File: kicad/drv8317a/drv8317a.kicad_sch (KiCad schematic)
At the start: 0 parts

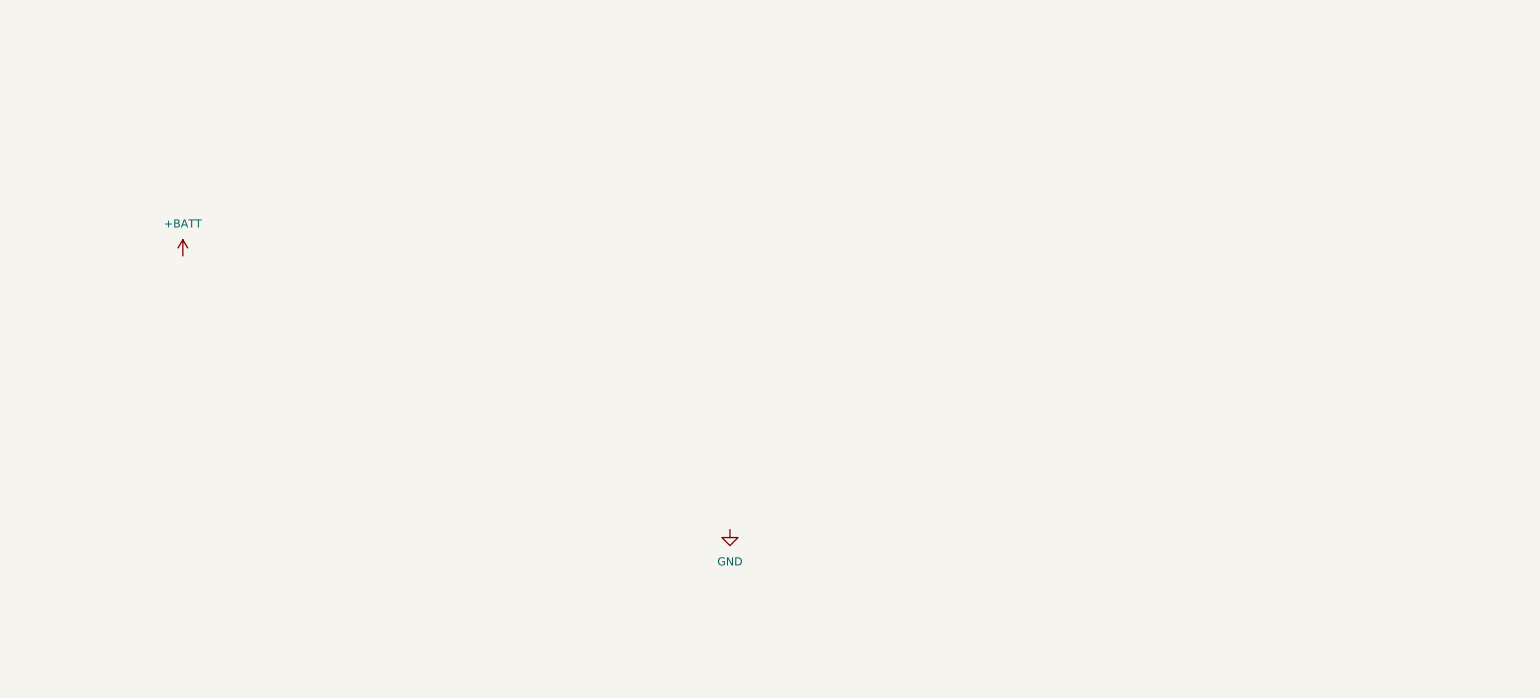
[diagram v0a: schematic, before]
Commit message: added DRV8317
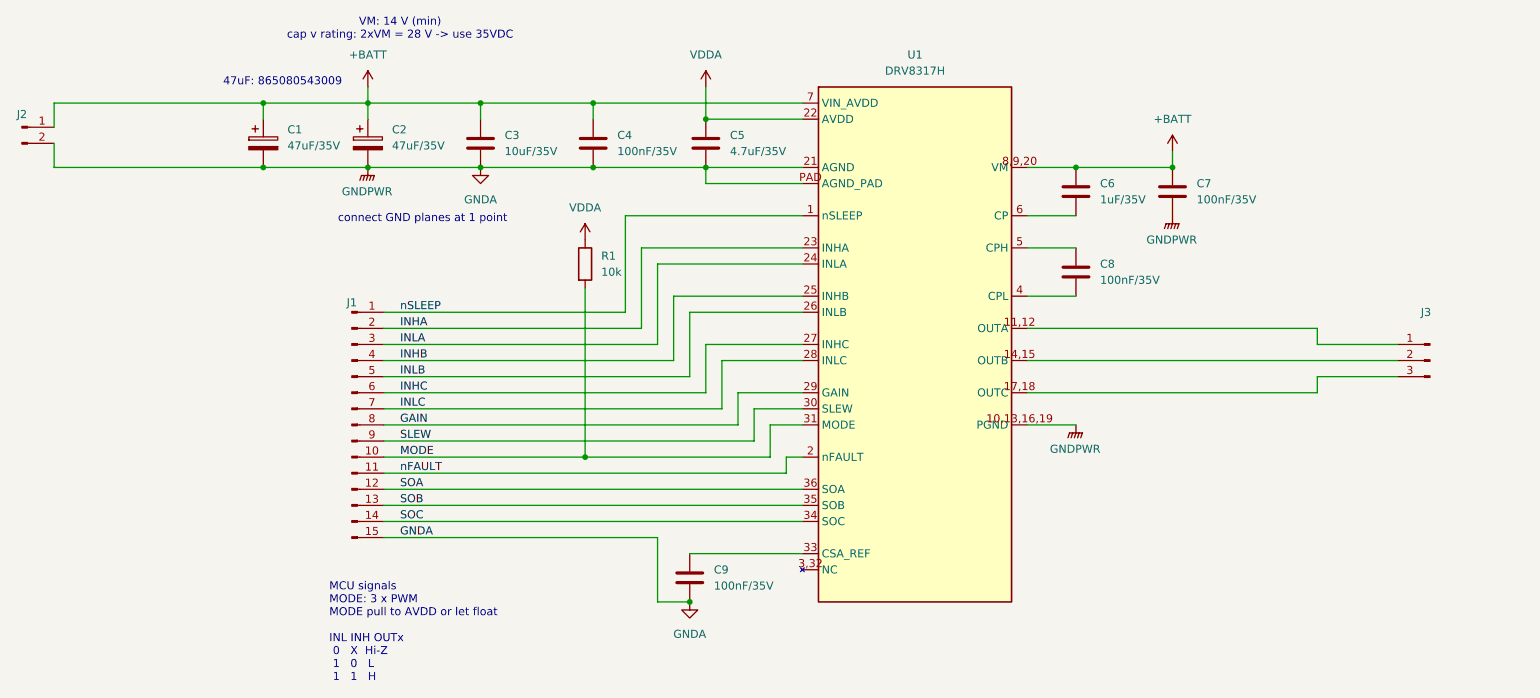
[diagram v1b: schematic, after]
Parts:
- added C1, C2: 47uF/35V, symbol Device:C_Polarized
- added C3: 10uF/35V, symbol Device:C
- added C4, C7, C8, C9: 100nF/35V, symbol Device:C
- added C5: 4.7uF/35V, symbol Device:C
- added C6: 1uF/35V, symbol Device:C
- added J1: Conn_01x15_Pin, symbol Connector:Conn_01x15_Pin
- added J2: Conn_01x02_Pin, symbol Connector:Conn_01x02_Pin
- added J3: Conn_01x03_Pin, symbol Connector:Conn_01x03_Pin
- added R1: 10k, symbol Device:R
- added U1: DRV8317H, symbol bldc-driver-lib:DRV8317H
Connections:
- net +BATT: now also C1.1, C2.1, C3.1, C4.1, C6.1, C7.1, J2.1 (Pin_1), U1.7 (VIN_AVDD), U1.8,9,20 (VM)
- new net: C6.2, U1.6 (CP)
- new net: J3.1 (Pin_1), U1.11,12 (OUTA)
- new net: J3.2 (Pin_2), U1.14,15 (OUTB)
- new net: J3.3 (Pin_3), U1.17,18 (OUTC)
- new net: C9.1, U1.33 (CSA_REF)
- new net: C8.2, U1.4 (CPL)
- new net: C8.1, U1.5 (CPH)
- new net GAIN: J1.8 (Pin_8), U1.29 (GAIN)
- new net GNDA: C1.2, C2.2, C3.2, C4.2, C5.2, C7.2, C9.2, J1.15 (Pin_15), J2.2 (Pin_2), U1.10,13,16,19 (PGND), U1.21 (AGND), U1.PAD (AGND_PAD)
- new net INHA: J1.2 (Pin_2), U1.23 (INHA)
- new net INHB: J1.4 (Pin_4), U1.25 (INHB)
- new net INHC: J1.6 (Pin_6), U1.27 (INHC)
- new net INLA: J1.3 (Pin_3), U1.24 (INLA)
- new net INLB: J1.5 (Pin_5), U1.26 (INLB)
- new net INLC: J1.7 (Pin_7), U1.28 (INLC)
- new net MODE: J1.10 (Pin_10), R1.2, U1.31 (MODE)
- new net SLEW: J1.9 (Pin_9), U1.30 (SLEW)
- new net SOA: J1.12 (Pin_12), U1.36 (SOA)
- new net SOB: J1.13 (Pin_13), U1.35 (SOB)
- new net SOC: J1.14 (Pin_14), U1.34 (SOC)
- new net VDDA: C5.1, R1.1, U1.22 (AVDD)
- new net nFAULT: J1.11 (Pin_11), U1.2 (nFAULT)
- new net nSLEEP: J1.1 (Pin_1), U1.1 (nSLEEP)
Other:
- note added: "47uF: 865080543009"
- note added: "MCU signals MODE: 3 x PWM MODE pull to AVDD or let float INL INH OUTx 0 X Hi-Z 1 0 L 1 1 H"
- note added: "VM: 14 V (min) cap v rating: 2xVM = 28 V -> use 35VDC"
- note added: "connect GND planes at 1 point"

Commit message: WQFN 36 Footprint added
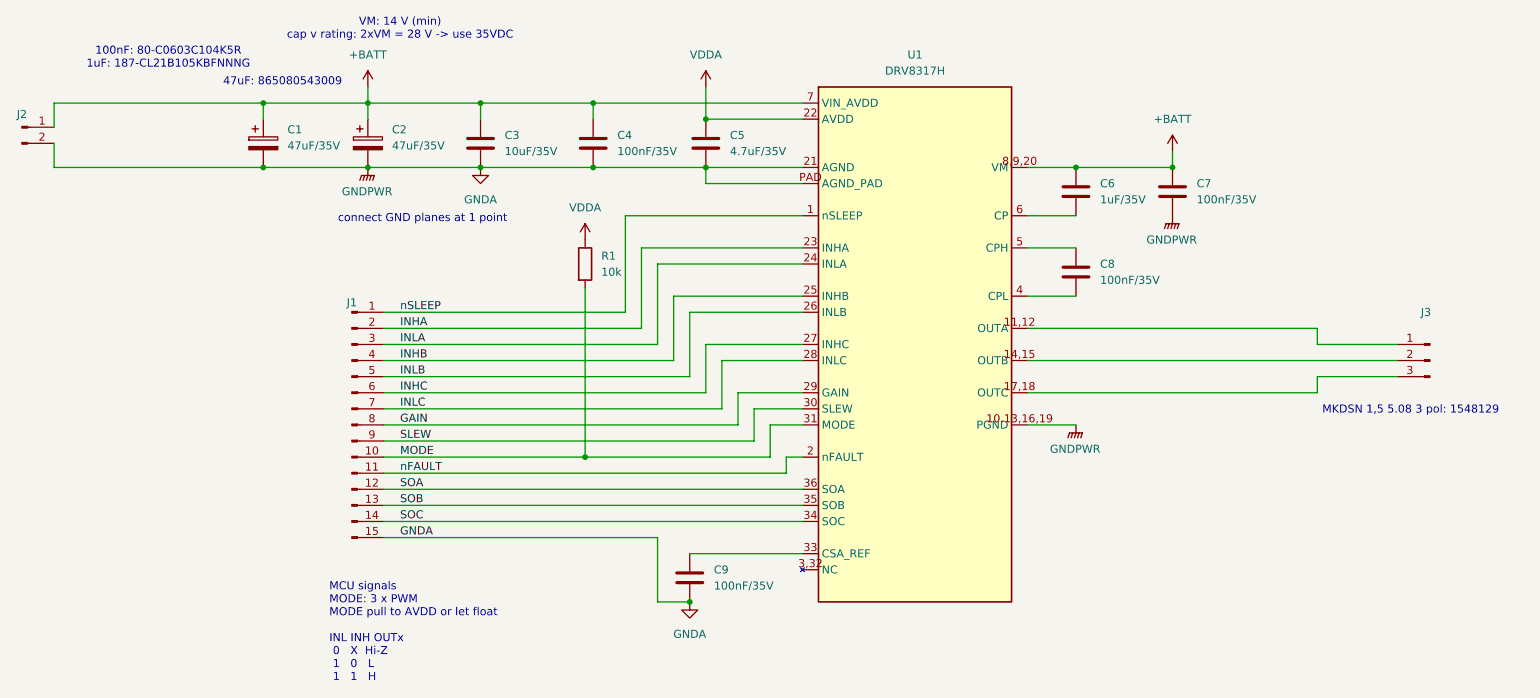
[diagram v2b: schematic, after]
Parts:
- C1, C2: footprint (none) -> Capacitor_SMD:CP_Elec_6.3x7.7
- C3, C5, C6: footprint (none) -> Capacitor_SMD:C_0805_2012Metric_Pad1.18x1.45mm_HandSolder
- C4, C7, C8, C9: footprint (none) -> Capacitor_SMD:C_0603_1608Metric_Pad1.08x0.95mm_HandSolder
- J1: footprint (none) -> Connector_PinHeader_2.54mm:PinHeader_1x15_P2.54mm_Vertical
- J2: footprint (none) -> Connector_PinHeader_2.54mm:PinHeader_1x02_P2.54mm_Vertical
- J3: footprint (none) -> TerminalBlock_Phoenix:TerminalBlock_Phoenix_MKDS-1,5-3-5.08_1x03_P5.08mm_Horizontal
- R1: footprint (none) -> Resistor_SMD:R_0603_1608Metric_Pad0.98x0.95mm_HandSolder
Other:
- note added: "100nF: 80-C0603C104K5R 1uF: 187-CL21B105KBFNNNG"
- note added: "MKDSN 1,5 5.08 3 pol: 1548129"
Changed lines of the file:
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@@
+		)
+	)
+	(text "MKDSN 1,5 5.08 3 pol: 1548129"
+		(exclude_from_sim no)
+		(at 245.872 94.234 0)
+		(effects
+			(font
+				(size 1.27 1.27)
+			)
 		)
 	)
@@
 		(exclude_from_sim no)
 		(at 67.818 42.418 0)
+		(effects
+			(font
+				(size 1.27 1.27)
+			)
+		)
+	)
+	(text "100nF: 80-C0603C104K5R\n1uF: 187-CL21B105KBFNNNG\n"
+		(exclude_from_sim no)
+		(at 49.784 38.608 0)
 		(effects
 			(font
@@
 			)
 		)
-		(property "Footprint" ""
+		(property "Footprint" "Capacitor_SMD:CP_Elec_6.3x7.7"
 			(at 65.7352 55.88 0)
 			(effects
@@
 			)
 		)
-		(property "Footprint" ""
+		(property "Footprint" "Capacitor_SMD:C_0805_2012Metric_Pad1.18x1.45mm_HandSolder"
 			(at 194.0052 63.5 0)
 			(effects
@@
 			)
 		)
-		(property "Footprint" ""
+		(property "Footprint" "Capacitor_SMD:C_0603_1608Metric_Pad1.08x0.95mm_HandSolder"
 			(at 117.8052 55.88 0)
 			(effects
@@
 			)
 		)
-		(property "Footprint" ""
+		(property "Footprint" "TerminalBlock_Phoenix:TerminalBlock_Phoenix_MKDS-1,5-3-5.08_1x03_P5.08mm_Horizontal"
 			(at 248.92 86.36 0)
 			(effects
@@
 			)
 		)
-		(property "Footprint" ""
+		(property "Footprint" "Capacitor_SMD:C_0805_2012Metric_Pad1.18x1.45mm_HandSolder"
 			(at 135.5852 55.88 0)
 			(effects
@@
 			)
 		)
-		(property "Footprint" ""
+		(property "Footprint" "Capacitor_SMD:C_0603_1608Metric_Pad1.08x0.95mm_HandSolder"
 			(at 209.2452 63.5 0)
 			(effects
@@
 			)
 		)
-		(property "Footprint" ""
+		(property "Footprint" "Connector_PinHeader_2.54mm:PinHeader_1x15_P2.54mm_Vertical"
 			(at 78.74 96.52 0)
 			(effects
@@
 			)
 		)
-		(property "Footprint" ""
+		(property "Footprint" "Capacitor_SMD:C_0603_1608Metric_Pad1.08x0.95mm_HandSolder"
 			(at 133.0452 124.46 0)
 			(effects
@@
 			)
 		)
-		(property "Footprint" ""
+		(property "Footprint" "Capacitor_SMD:CP_Elec_6.3x7.7"
 			(at 82.2452 55.88 0)
 			(effects
@@
 			)
 		)
-		(property "Footprint" ""
+		(property "Footprint" "Capacitor_SMD:C_0805_2012Metric_Pad1.18x1.45mm_HandSolder"
 			(at 100.0252 55.88 0)
 			(effects
@@
 			)
 		)
-		(property "Footprint" ""
+		(property "Footprint" "Resistor_SMD:R_0603_1608Metric_Pad0.98x0.95mm_HandSolder"
 			(at 113.792 71.12 90)
 			(effects
@@
 			)
 		)
-		(property "Footprint" ""
+		(property "Footprint" "Connector_PinHeader_2.54mm:PinHeader_1x02_P2.54mm_Vertical"
 			(at 26.67 49.53 0)
 			(effects
@@
 			)
 		)
-		(property "Footprint" ""
+		(property "Footprint" "Capacitor_SMD:C_0603_1608Metric_Pad1.08x0.95mm_HandSolder"
 			(at 194.0052 76.2 0)
 			(effects

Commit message: pcb started
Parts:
- removed C2: 47uF/35V, Capacitor_SMD:CP_Elec_6.3x7.7, symbol Device:C_Polarized
- removed J1: Conn_01x15_Pin, Connector_PinHeader_2.54mm:PinHeader_1x15_P2.54mm_Vertical, symbol Connector:Conn_01x15_Pin
- added J1: Conn_01x08_Pin, Connector_PinHeader_2.54mm:PinHeader_1x08_P2.54mm_Vertical, symbol Connector:Conn_01x08_Pin
- added J4: Conn_01x06_Pin, Connector_PinHeader_2.54mm:PinHeader_1x06_P2.54mm_Vertical, symbol Connector:Conn_01x06_Pin
- added NT1: NetTie_2, NetTie:NetTie-2_SMD_Pad2.0mm, symbol Device:NetTie_2
- U1: footprint (none) -> bldc-driver-lib:WQFN-36_EP_4.4x5.4_Pitch0.4mm
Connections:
- net INLB is gone; now on net INL: U1.26 (INLB)
- net INLC is gone; now on net INL: U1.28 (INLC)
- net +BATT: now also U1.20 (VM), U1.8 (VM), U1.9 (VM); no longer U1.8,9,20 (VM)
- net GAIN: now also J1.6 (Pin_6)
- net GNDA: now also U1.37 (AGND_PAD), J4.5 (Pin_5), J4.6 (Pin_6), NT1.2; no longer C1.2, C7.2, J2.2 (Pin_2), U1.10,13,16,19 (PGND), U1.PAD (AGND_PAD)
- net INHA: now also J1.2 (Pin_2)
- net INHB: now also J1.3 (Pin_3)
- net INHC: now also J1.4 (Pin_4)
- net MODE: now also J1.8 (Pin_8)
- net SLEW: now also J1.7 (Pin_7)
- net SOA: now also J4.2 (Pin_2)
- net SOB: now also J4.3 (Pin_3)
- net SOC: now also J4.4 (Pin_4)
- net nFAULT: now also J4.1 (Pin_1)
- net nSLEEP: now also J1.1 (Pin_1)
- net OUTA: now reaches J3.1 (Pin_1)
- net OUTA: now also U1.11 (OUTA), U1.12 (OUTA); no longer U1.11,12 (OUTA)
- net OUTB: now reaches J3.2 (Pin_2)
- net OUTB: now also U1.14 (OUTB), U1.15 (OUTB); no longer U1.14,15 (OUTB)
- net OUTC: now reaches J3.3 (Pin_3)
- net OUTC: now also U1.17 (OUTC), U1.18 (OUTC); no longer U1.17,18 (OUTC)
- net INLA renamed INL
- net INL: now also J1.5 (Pin_5)
- new net GNDPWR: C1.2, C7.2, J2.2 (Pin_2), NT1.1, U1.10 (PGND), U1.13 (PGND), U1.16 (PGND), U1.19 (PGND)
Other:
- moved on the sheet: C1, J2, J3, R1

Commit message: 100% routed, review needed
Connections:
- net GAIN: now also J1.5 (Pin_5); no longer J1.6 (Pin_6)
- net INHA: now also J1.1 (Pin_1); no longer J1.2 (Pin_2)
- net INHB: now also J1.2 (Pin_2); no longer J1.3 (Pin_3)
- net INHC: now also J1.3 (Pin_3); no longer J1.4 (Pin_4)
- net INL: now also J1.4 (Pin_4); no longer J1.5 (Pin_5)
- net MODE: now also J1.7 (Pin_7); no longer J1.8 (Pin_8)
- net SLEW: now also J1.6 (Pin_6); no longer J1.7 (Pin_7)
- net nSLEEP: now also J1.8 (Pin_8); no longer J1.1 (Pin_1)

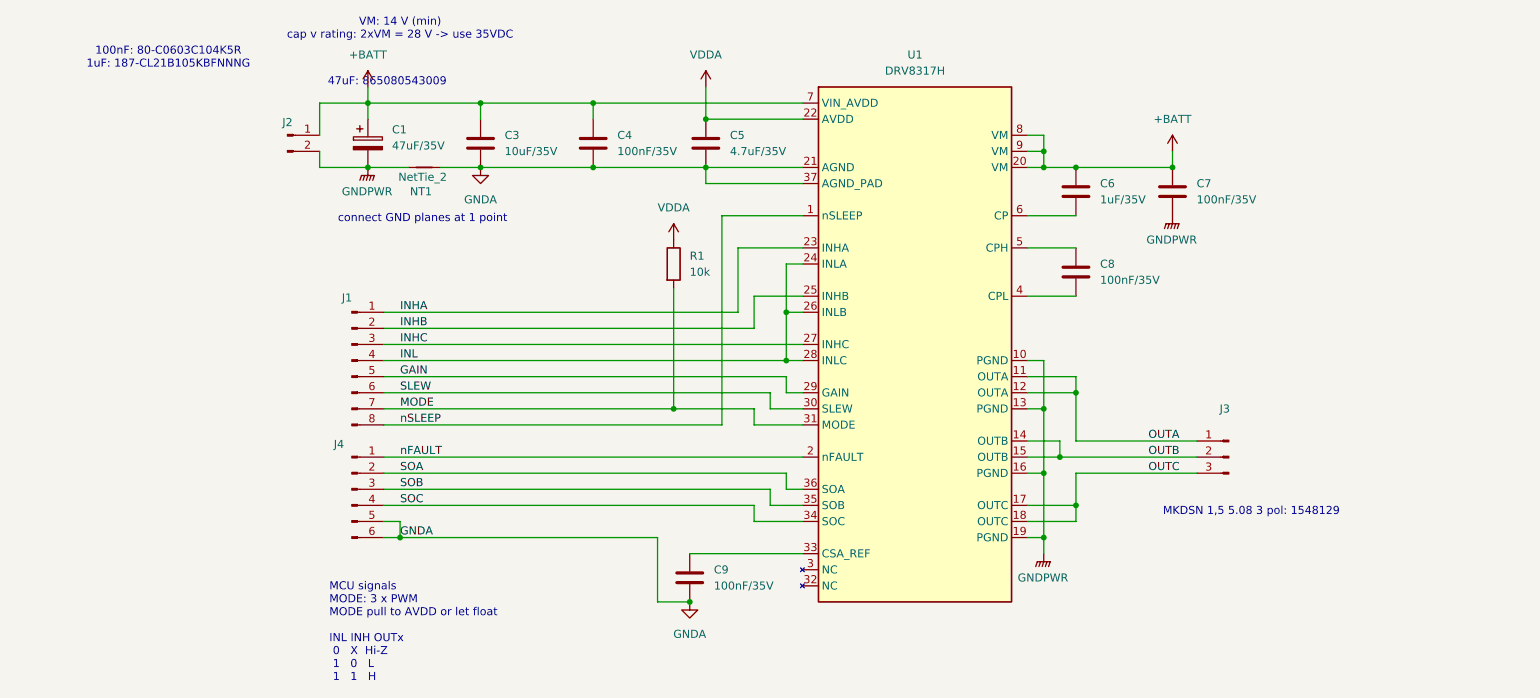
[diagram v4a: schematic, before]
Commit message: config: use resistors instead of mcu signals
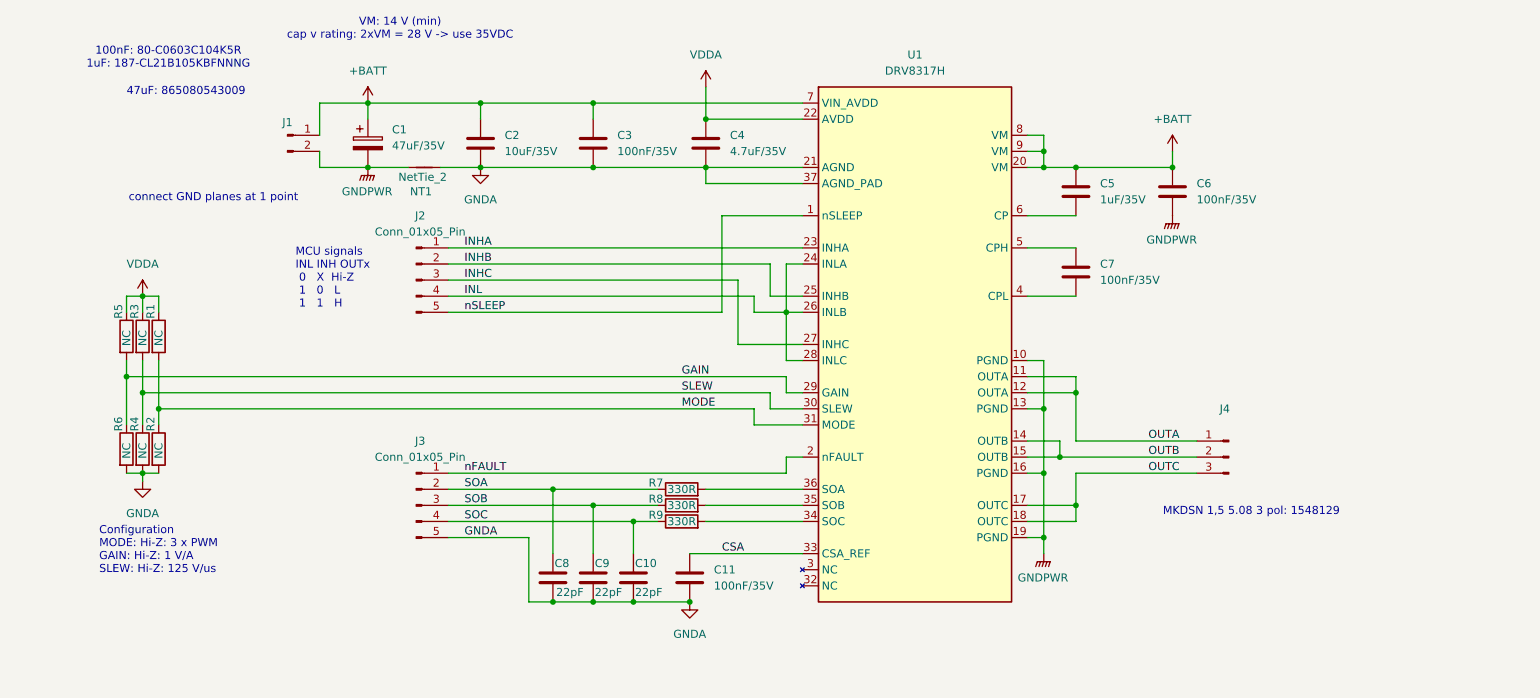
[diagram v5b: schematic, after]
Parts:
- removed J1: Conn_01x08_Pin, Connector_PinHeader_2.54mm:PinHeader_1x08_P2.54mm_Vertical, symbol Connector:Conn_01x08_Pin
- removed J4: Conn_01x06_Pin, Connector_PinHeader_2.54mm:PinHeader_1x06_P2.54mm_Vertical, symbol Connector:Conn_01x06_Pin
- added C10, C8, C9: 22pF, Capacitor_SMD:C_0603_1608Metric_Pad1.08x0.95mm_HandSolder, symbol Device:C
- added J2, J3: Conn_01x05_Pin, Connector_PinHeader_2.54mm:PinHeader_1x05_P2.54mm_Vertical, symbol Connector:Conn_01x05_Pin
- added R2, R3, R4, R5, R6: NC, Resistor_SMD:R_0603_1608Metric_Pad0.98x0.95mm_HandSolder, symbol Device:R
- added R7, R8, R9: 330R, Resistor_SMD:R_0603_1608Metric_Pad0.98x0.95mm_HandSolder, symbol Device:R
- R1: value 10k -> NC
- renumbered C9 to C11, C3 to C2, C4 to C3, C5 to C4, C6 to C5, C7 to C6, C8 to C7, J2 to J1, J3 to J4
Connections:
- net GAIN: now also R5.2, R6.1
- net GNDA: now also C10.2, C8.2, C9.2, J3.5 (Pin_5), R2.2, R4.2, R6.2
- net INHA: now also J2.1 (Pin_1)
- net INHB: now also J2.2 (Pin_2)
- net INHC: now also J2.3 (Pin_3)
- net INL: now also J2.4 (Pin_4)
- net MODE: now also R2.1
- net SLEW: now also R3.2, R4.1
- net SOA: now also C8.1, J3.2 (Pin_2), R7.1; no longer U1.36 (SOA)
- net SOB: now also C9.1, J3.3 (Pin_3), R8.1; no longer U1.35 (SOB)
- net SOC: now also C10.1, J3.4 (Pin_4), R9.1; no longer U1.34 (SOC)
- net VDDA: now also R3.1, R5.1
- net nFAULT: now also J3.1 (Pin_1)
- net nSLEEP: now also J2.5 (Pin_5)
- net CSA: now reaches C11.1, U1.33 (CSA_REF)
- new net: R9.2, U1.34 (SOC)
- new net: R8.2, U1.35 (SOB)
- new net: R7.2, U1.36 (SOA)
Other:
- note added: "Configuration MODE: Hi-Z: 3 x PWM GAIN: Hi-Z: 1 V/A SLEW: Hi-Z: 125 V/us"
- note added: "MCU signals INL INH OUTx 0 X Hi-Z 1 0 L 1 1 H"
- note removed: "MCU signals MODE: 3 x PWM MODE pull to AVDD or let float INL INH OUTx 0 X Hi-Z 1 0 L 1 1 H"
